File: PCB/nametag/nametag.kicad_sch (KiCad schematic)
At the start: 8 parts, among them J1 USB_C_Receptacle_USB2.0_14P, U1 AVR64DU32, U2 TPS70633DBVR

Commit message: Schematic complete
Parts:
- removed U2: TPS70633DBVR, symbol Nametag Sch Library:TPS706
- added C10, C11, C12, C4, C6, C7, C8, C9: 1uF, 25V, Capacitor_SMD:C_0805_2012Metric_Pad1.18x1.45mm_HandSolder, symbol Device:C_Small
- added C13, C14, C15, C16, C18, C19, C3: 0.1uF, 16V, Capacitor_SMD:C_0805_2012Metric_Pad1.18x1.45mm_HandSolder, symbol Device:C_Small
- added C17: 10nF, Capacitor_SMD:C_0805_2012Metric_Pad1.18x1.45mm_HandSolder, symbol Device:C_Small
- added C5: 4.7uF/25V, Capacitor_SMD:C_0805_2012Metric_Pad1.18x1.45mm_HandSolder, symbol Device:C_Small
- added CLR0, CLR1, CLR2, SIZE0, SIZE1, SIZE2, SIZE3: 0, Resistor_SMD:R_0603_1608Metric_Pad0.98x0.95mm_HandSolder, symbol Device:R_Small_US
- added D1, D2, D3: PMEG3020ER, StandardPackages_Custom:SOD-123W, symbol Device:D_Schottky
- added J2: ~, nametag:FH34SRJ-24S-0.5SH, symbol Nametag Sch Library:EPAPER_24
- added J3: Conn_02x03_Odd_Even, StandardPackages_Custom:TC2030-IDC-FP, symbol Connector_Generic:Conn_02x03_Odd_Even
- added L1: 10uH, Inductor_SMD:L_1008_2520Metric_Pad1.43x2.20mm_HandSolder, symbol Device:L_Small
- added Q1: NXV55UN, StandardPackages_Custom:SOT23-3, symbol Device:Q_NMOS_GSD
- added R4: 0.47, 0.5W, Resistor_SMD:R_1206_3216Metric_Pad1.30x1.75mm_HandSolder, symbol Device:R_Small_US
- added R6: 100k, Resistor_SMD:R_0805_2012Metric_Pad1.20x1.40mm_HandSolder, symbol Device:R_Small_US
- added U1: MIC550x, StandardPackages_Custom:SOT23-5, symbol Nametag Sch Library:MIC5501/4
- added U3: 23K640, StandardPackages_Custom:SOIC-8, symbol Nametag Sch Library:23K640
- added U4: MCP9700x-ETT, Package_TO_SOT_SMD:SOT-23, symbol Sensor_Temperature:MCP9700x-ETT
- added U5, U6: SN74LV1T125DBV, Package_TO_SOT_SMD:SOT-23-5, symbol Logic_LevelTranslator:SN74LV1T125DBV
- C1: value 1uF -> 1uF, 25V; footprint (none) -> Capacitor_SMD:C_0805_2012Metric_Pad1.18x1.45mm_HandSolder
- C2: footprint (none) -> Capacitor_SMD:C_0805_2012Metric_Pad1.18x1.45mm_HandSolder
- J1: footprint (none) -> nametag:12402012E212A
- R1: renamed from R3; footprint (none) -> Resistor_SMD:R_0805_2012Metric_Pad1.20x1.40mm_HandSolder; now fitted
- R2: renamed from R1; footprint (none) -> Resistor_SMD:R_0805_2012Metric_Pad1.20x1.40mm_HandSolder
- renumbered R2 to R3, U1 to U2
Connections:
- net +3.3V: now also U2.28 (VDD), C13.1, C14.1, C16.1, C17.1, C18.1, C19.1, C3.1, C4.1, J2.15 (VDDIO), J2.16 (VDDA), J3.2 (Pin_2), L1.1, U1.5 (OUT), U3.7 (~{HOLD}), U3.8 (VCC), U4.1 (V_{DD}), U5.5 (VCC), U6.5 (VCC)
- net +5V: now also U1.1 (IN), U1.3 (EN)
- net GND: now also U2.29 (VSS), C10.1, C11.1, C12.1, C13.2, C14.2, C15.2, C16.2, C17.2, C18.2, C19.2, C3.2, C4.2, C6.1, C7.1, C8.1, C9.1, CLR0.1, CLR1.1, CLR2.1, D2.1 (K), J2.17 (GND), J2.8 (BS), J3.6 (Pin_6), R4.1, R6.2, SIZE0.1, SIZE1.1, SIZE2.1, SIZE3.1, U1.2 (GND), U1.4 (NC), U3.4 (VSS), U4.3 (GND), U5.3 (GND), U6.3 (GND)
- net ~{DISP_MISO_EN}: now reaches U2.1 (PA3)
- net ~{DISP_MISO_EN}: now also U6.1 (~{OE})
- net at U2.10 (PD0): now also SIZE1.2
- net at U2.11 (PD1): now also SIZE2.2
- net at U2.12 (PD2): now also SIZE3.2
- net D/C: now reaches U2.13 (PD3)
- net D/C: now also J2.11 (D/C)
- net MOSI: now reaches U2.2 (PA4)
- net MOSI: now also U3.2 (SO), U6.2 (A)
- net at U2.20 (PF0): now also CLR0.2
- net at U2.21 (PF1): now also CLR1.2
- net at U2.22 (PF2): now also CLR2.2
- net ~{FLASH_CS}: now reaches U2.23 (PF3)
- net ~{FLASH_CS}: now also U3.1 (~{CS})
- net ~{DISP_RESET}: now reaches U2.24 (PF4)
- net ~{DISP_RESET}: now also J2.10 (~{RESET})
- net ~{BUSY}: now reaches U2.25 (PF5)
- net ~{BUSY}: now also J2.9 (~{BUSY})
- net ~{RESET}: now reaches U2.26 (PF6/~{RESET})
- net ~{RESET}: now also C15.1, J3.5 (Pin_5)
- net UPDI: now reaches U2.27 (PF7/UPDI)
- net UPDI: now also J3.1 (Pin_1)
- net MISO: now reaches U2.3 (PA5)
- net MISO: now also U3.5 (SI), U5.4 (Y)
- net TEMP: now reaches U2.32 (PA2)
- net TEMP: now also U4.2 (V_{OUT})
- net SCLK: now reaches U2.4 (PA6)
- net SCLK: now also J2.13 (SCLK/SCL), U3.6 (SCLK)
- net ~{DISP_CS}: now reaches U2.5 (PA7)
- net ~{DISP_CS}: now also J2.12 (~{CS}), U5.1 (~{OE})
- net at U2.9 (PC3): now also SIZE0.2
- new net: C7.2, J2.20 (VDH)
- new net: J2.3 (RESE), Q1.2 (S), R4.2
- new net: C5.1, D2.2 (A), D3.1 (K)
- new net: C5.2, D1.2 (A), L1.2, Q1.3 (D)
- new net: C12.2, D3.2 (A), J2.23 (VGL)
- new net: C8.2, J2.22 (VDL)
- new net: J2.2 (GDR), Q1.1 (G)
- new net: C6.2, D1.1 (K), J2.21 (VGH)
- new net: C10.2, J2.18 (VDDD)
- new net: C9.2, J2.24 (VCOM)
- new net: C11.2, J2.5 (VDHR)
- new net SDA: J2.14 (SDI/SDA), R6.1, U5.2 (A), U6.4 (Y)
- no-connect marks 0 -> 13
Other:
- moved on the sheet: C1, C2, J1, R2, R3, U2

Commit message: PCB WIP
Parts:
- added C20, C21, C22: 10uF, Capacitor_SMD:C_1206_3216Metric_Pad1.33x1.80mm_HandSolder, symbol Device:C_Small
- added C23: 0.1uF, 16V, Capacitor_SMD:C_0805_2012Metric_Pad1.18x1.45mm_HandSolder, symbol Device:C_Small
- added D4, D5, D6: LED, StandardPackages_Custom:LED 0805, symbol Device:LED
- added R5, R7, R8: 470, Resistor_SMD:R_0805_2012Metric_Pad1.20x1.40mm_HandSolder, symbol Device:R_Small_US
- added R9: 0, Resistor_SMD:R_0603_1608Metric_Pad0.98x0.95mm_HandSolder, symbol Device:R_Small_US
- C19: now not fitted
- R3: footprint Resistor_SMD:R_0805_2012Metric -> Resistor_SMD:R_0805_2012Metric_Pad1.20x1.40mm_HandSolder
- U4: footprint Package_TO_SOT_SMD:SOT-23 -> StandardPackages_Custom:SOT23-3; now not fitted
- U5, U6: footprint Package_TO_SOT_SMD:SOT-23-5 -> StandardPackages_Custom:SOT23-5
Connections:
- net +3.3V: now also C20.2, C21.2, C22.2, C23.1, R9.1
- net D/C: now also U2.30 (PA0); no longer U2.13 (PD3)
- net GND: now also J1.S1 (SHIELD), R1.1, C20.1, C21.1, C22.1, C23.2, R5.1, R7.1, R8.1
- net TEMP: now also U2.17 (PD7); no longer U2.32 (PA2)
- net ~{BUSY}: now also U2.32 (PA2); no longer U2.25 (PF5)
- net ~{DISP_RESET}: now also U2.31 (PA1); no longer U2.24 (PF4)
- net at CLR0.2: now also U2.14 (PD4); no longer U2.20 (PF0)
- net at CLR1.2: now also U2.15 (PD5); no longer U2.21 (PF1)
- net at U3.3 (NC): now also R9.2
- net at CLR2.2: now also U2.16 (PD6); no longer U2.22 (PF2)
- new net: D5.1 (K), R7.2
- new net: D4.1 (K), R5.2
- new net: D6.1 (K), R8.2
- new net LED_DISP: D4.2 (A), U2.22 (PF2)
- new net LED_MEM: D5.2 (A), U2.21 (PF1)
- new net LED_USB: D6.2 (A), U2.20 (PF0)
- no-connect marks 13 -> 10
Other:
- moved on the sheet: C10, C11, C12, C13, C14, C15, C16, C17, C18, C3, C4, C5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

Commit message: PCB files. BOM. Step model.
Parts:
- removed C22: 10uF, Capacitor_SMD:C_1206_3216Metric_Pad1.33x1.80mm_HandSolder, symbol Device:C_Small
- C23: now not fitted
- J3: now left out of the parts list
- U3: footprint StandardPackages_Custom:SOIC-8 -> Microchip:TSSOP-8 (ST); now not fitted
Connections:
- net ~{DISP_CS}: now also U2.1 (PA3); no longer U2.5 (PA7)
- net ~{DISP_MISO_EN}: now also U2.24 (PF4); no longer U2.1 (PA3)
- net ~{FLASH_CS}: now also U2.5 (PA7); no longer U2.23 (PF3)
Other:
- moved on the sheet: C1, C10, C11, C12, C13, C14, C15, C16, C17, C18, C19, C2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

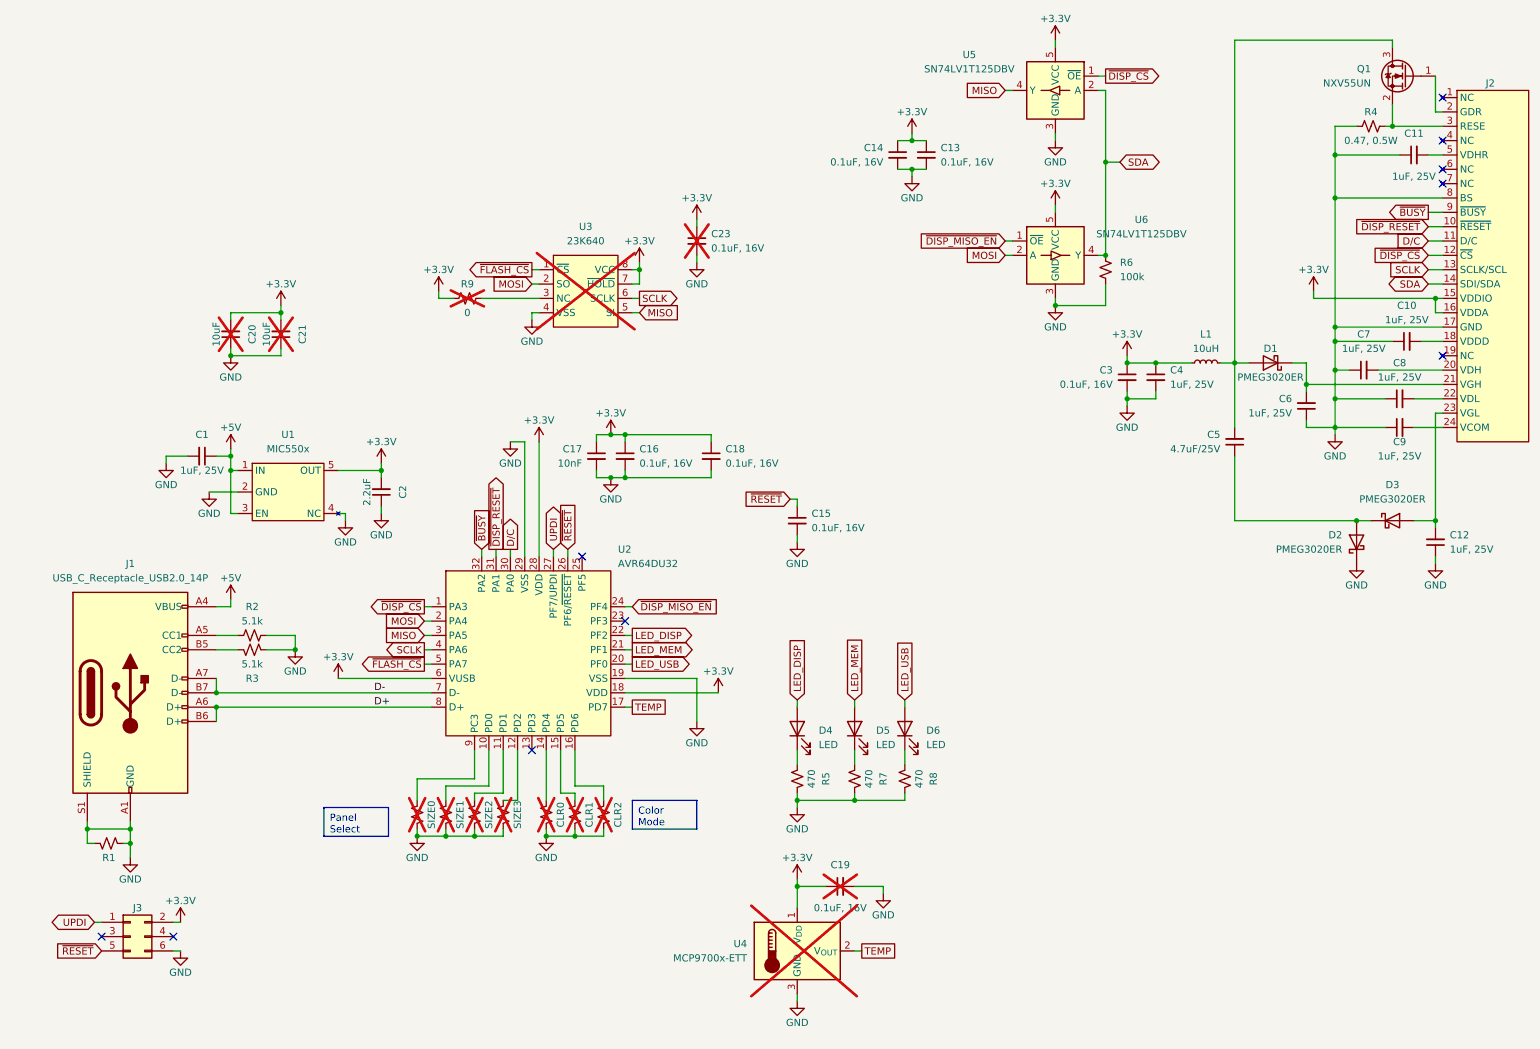
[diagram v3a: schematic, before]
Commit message: Created common SPI library
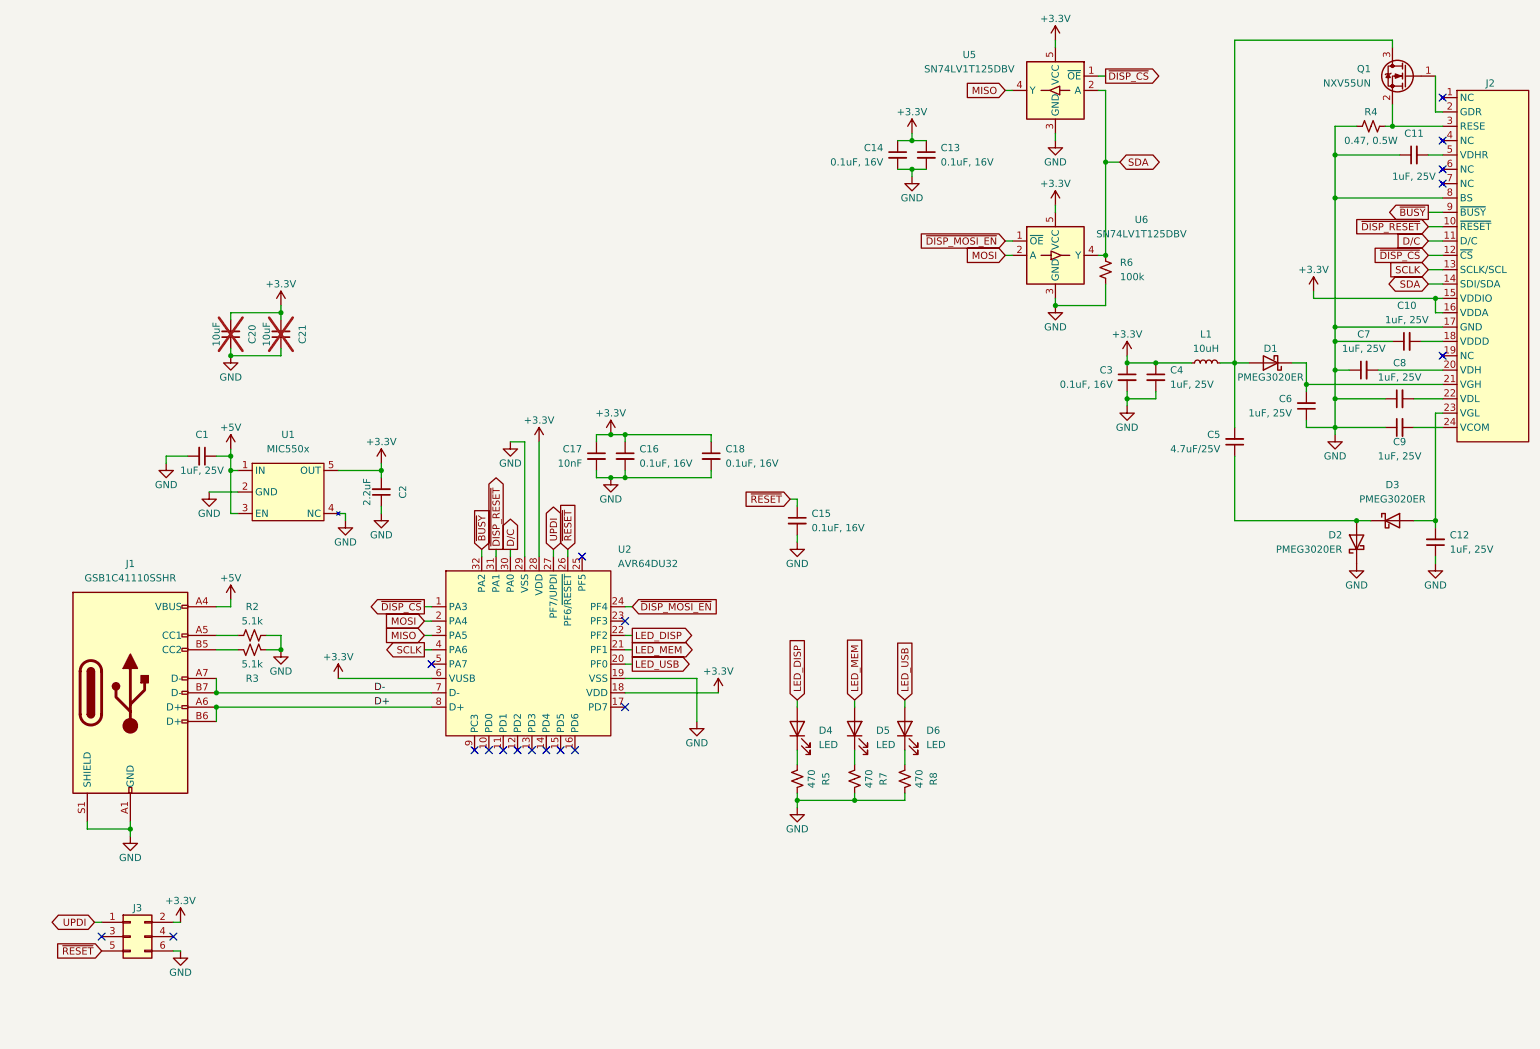
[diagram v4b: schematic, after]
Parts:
- removed C19, C23: 0.1uF, 16V, Capacitor_SMD:C_0805_2012Metric_Pad1.18x1.45mm_HandSolder, symbol Device:C_Small
- removed CLR0, CLR1, CLR2, R9, SIZE0, SIZE1, SIZE2, SIZE3: 0, Resistor_SMD:R_0603_1608Metric_Pad0.98x0.95mm_HandSolder, symbol Device:R_Small_US
- removed R1: 0, Resistor_SMD:R_0805_2012Metric_Pad1.20x1.40mm_HandSolder, symbol Device:R_Small_US
- removed U3: 23K640, Microchip:TSSOP-8 (ST), symbol Nametag Sch Library:23K640
- removed U4: MCP9700x-ETT, StandardPackages_Custom:SOT23-3, symbol Sensor_Temperature:MCP9700x-ETT
- J1: value USB_C_Receptacle_USB2.0_14P -> GSB1C41110SSHR; footprint nametag:12402012E212A -> nametag:GSB1C41110SSHR
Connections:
- net TEMP: no longer names the net of U2.17 (PD7)
- net ~{DISP_MISO_EN} renamed ~{DISP_MOSI_EN}
- net ~{FLASH_CS}: no longer names the net of U2.5 (PA7)
- no-connect marks 10 -> 19

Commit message: README edits. Added renders and BOM
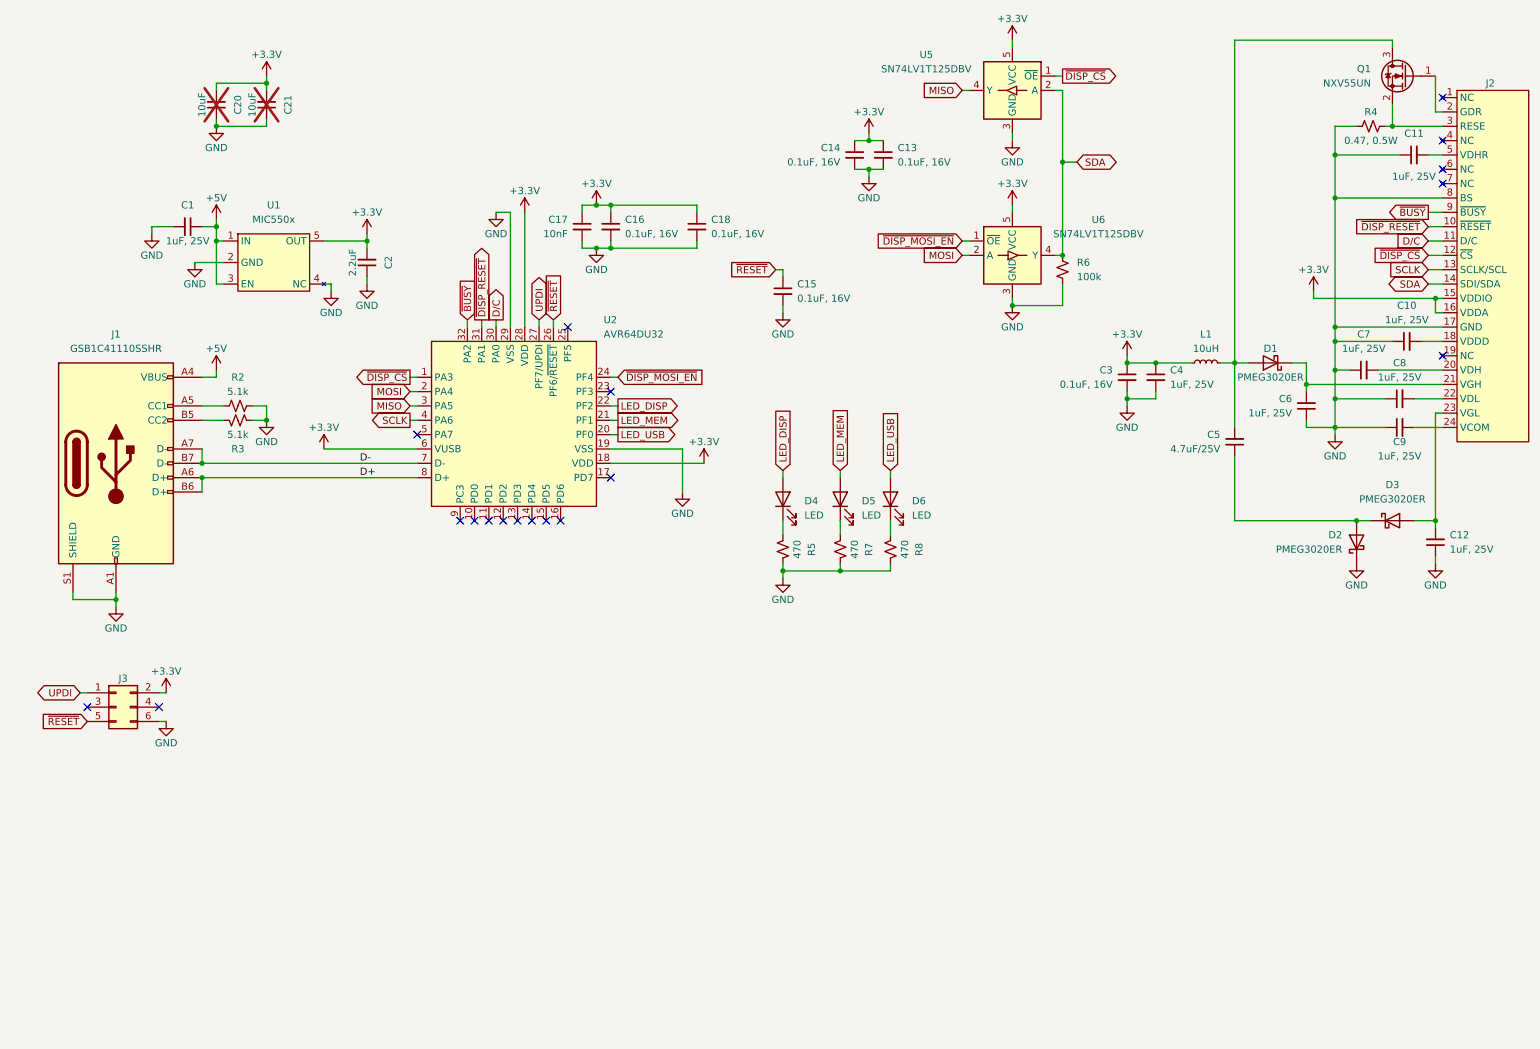
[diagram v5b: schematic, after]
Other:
- company: (none) -> Created by Robert Perkel
- title: (none) -> E-Paper Nametag
- moved on the sheet: C1, C13, C14, C15, C16, C17, C18, C2, C20, C21, D4, D5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
